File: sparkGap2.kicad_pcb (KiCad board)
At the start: 4 copper layers, 53.1 x 54.1 mm, 47 parts, among them J1 9V, J2 IN, J3 OUT, Q1 BS170, SW1 SPST, SW2 6-pin Footswitch, U1 TL072

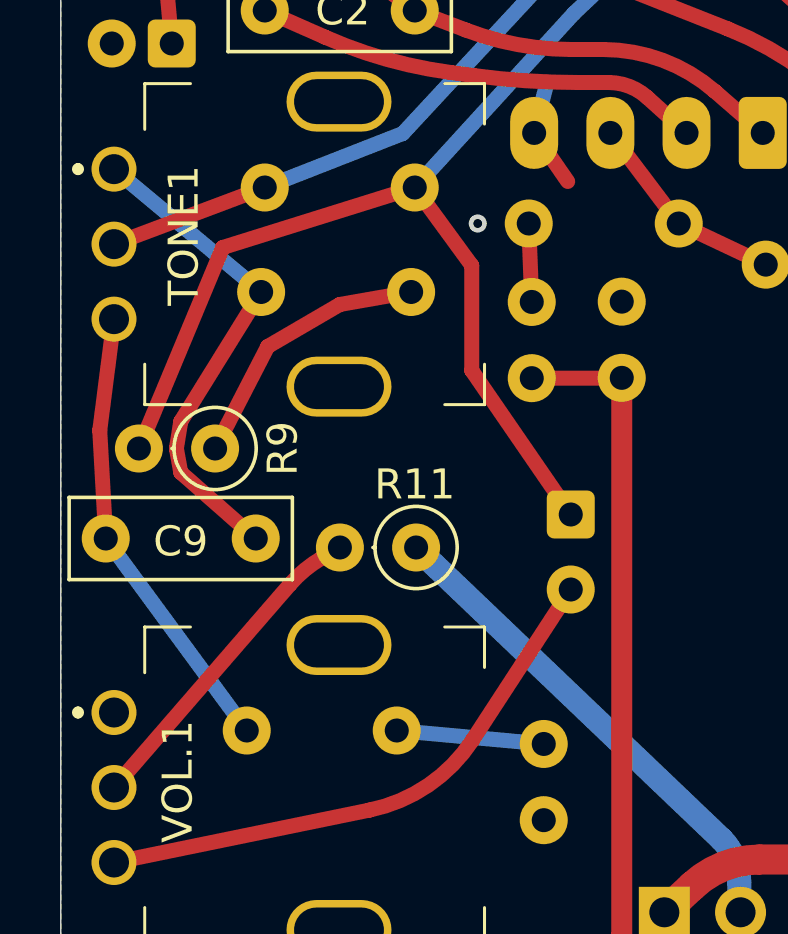
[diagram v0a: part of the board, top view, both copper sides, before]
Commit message: Tweak R placement under vol. pot. Round a few tracks
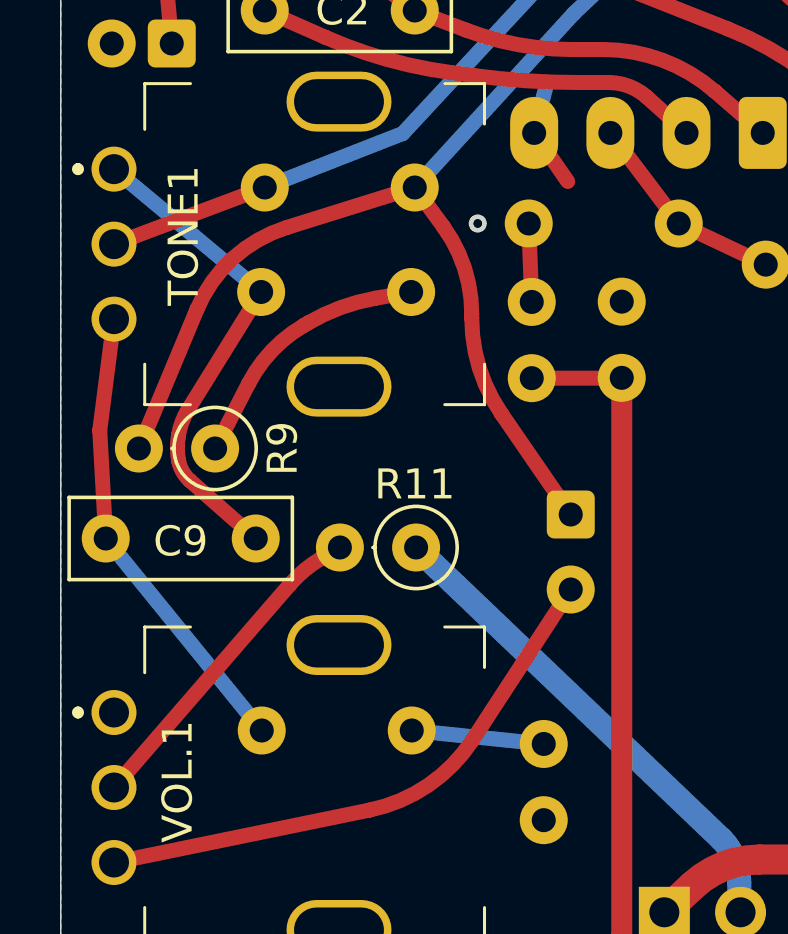
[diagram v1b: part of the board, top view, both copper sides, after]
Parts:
- moved C10 0.50 mm to (26.7, 83.0)
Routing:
- net Net-(C11-Pad1): track 42.7 -> 42.2 mm

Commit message: improved silkscreen, and component refs
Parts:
- D1: footprint Diode_THT:D_DO-41_SOD81_P2.54mm_Vertical_AnodeUp -> SamacSys_Parts:D_DO-41_SOD81_P2.54mm_Vertical_AnodeUp
- D4: footprint Diode_THT:D_DO-35_SOD27_P2.54mm_Vertical_AnodeUp -> SamacSys_Parts:D_DO-35_SOD27_P2.54mm_Vertical_AnodeUp
- R1, R10, R11, R12, R13, R14, R2, R3, R4, R5, R6, R8, R9: footprint Resistor_THT:R_Axial_DIN0207_L6.3mm_D2.5mm_P2.54mm_Vertical -> SamacSys_Parts:R_Axial_DIN0207_L6.3mm_D2.5mm_P2.54mm_Vertical
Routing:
- net 9V: track 18.4 -> 17.6 mm
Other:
- board text added: "v1.0 2026"
- board text removed: "v0.4 2026"
